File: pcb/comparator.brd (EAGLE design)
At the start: 15.9 x 15.6 mm, 13 parts, among them U1 MAX9032

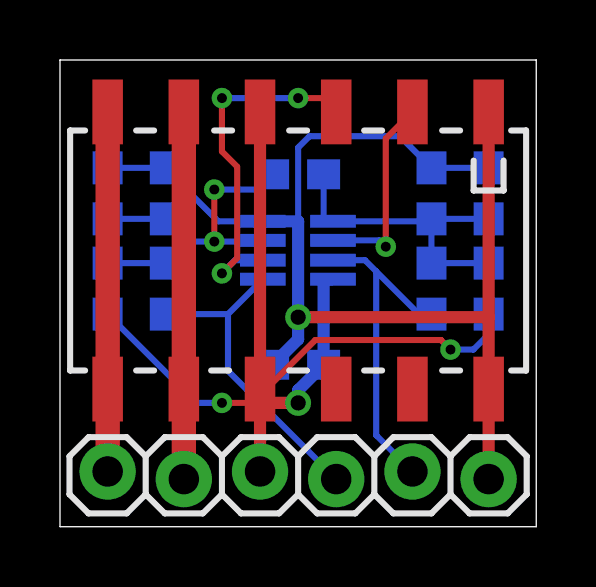
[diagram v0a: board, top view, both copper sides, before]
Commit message: Tweaked encoder conditiner board
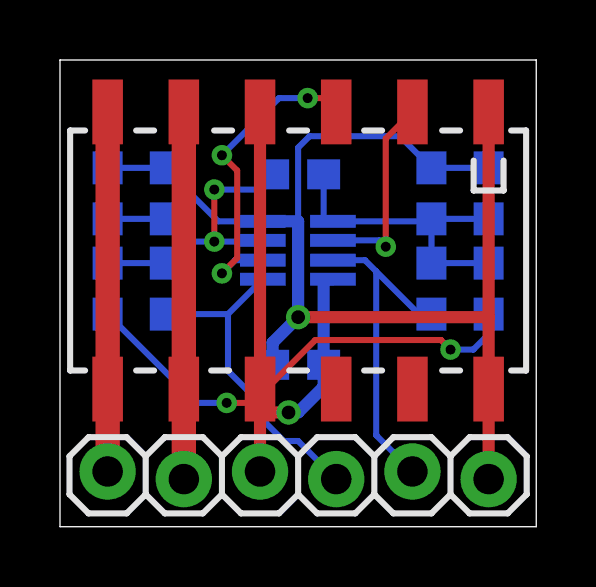
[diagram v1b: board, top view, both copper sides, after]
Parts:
- turned R4 to 90 degrees
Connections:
- net 3.3V: now also R4.1; no longer R4.2
- net N$6: now also R4.2; no longer R4.1
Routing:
- net EN2I: track 12.1 -> 11.0 mm
- net 3.3V: track 34.0 -> 34.8 mm
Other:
- board text added: "Encoder Conditioner"
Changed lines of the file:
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@@
 <setting verticaltext="up"/>
 </settings>
-<grid distance="0.05" unitdist="inch" unit="inch" style="lines" multiple="1" display="no" altdistance="0.0125" altunitdist="inch" altunit="inch"/>
+<grid distance="0.05" unitdist="inch" unit="inch" style="lines" multiple="1" display="no" altdistance="0.00625" altunitdist="inch" altunit="inch"/>
 <layers>
 <layer number="1" name="Top" color="4" fill="1" visible="yes" active="yes"/>
@@
 <wire x1="15.875" y1="15.5575" x2="0" y2="15.5575" width="0" layer="20"/>
 <wire x1="0" y1="15.5575" x2="0" y2="0" width="0" layer="20"/>
-<text x="14.2875" y="4.7625" size="0.8128" layer="22" rot="SMR270" align="center">GND</text>
-<text x="12.7" y="14.2875" size="0.8128" layer="22" rot="MR0" align="center">MAX9032</text>
+<text x="14.2875" y="4.445" size="0.8128" layer="22" rot="SMR270" align="center">GND</text>
+<text x="10.4775" y="6.6675" size="0.6096" layer="22" rot="MR270" align="center">MAX9032</text>
+<text x="11.7475" y="13.97" size="0.8128" layer="22" rot="MR0" align="center">Encoder
+Conditioner</text>
 </plain>
 <attributes>
@@
 </element>
 <element name="U1" library="Custom" package="SOT23-8" value="MAX9032" x="7.9375" y="9.2075" smashed="yes" rot="MR180">
-<attribute name="NAME" x="6.96514375" y="7.309653125" size="0.8128" layer="26" ratio="10" rot="SMR180"/>
+<attribute name="NAME" x="8.55264375" y="7.627153125" size="0.6096" layer="26" ratio="10" rot="SMR180"/>
 </element>
 <element name="R1" library="SparkFun-Resistors" package="0603-RES" value="10K" x="1.5875" y="7.9375" rot="MR270"/>
 <element name="R2" library="SparkFun-Resistors" package="0603-RES" value="3.3K" x="3.4925" y="11.1125" rot="MR90"/>
 <element name="R3" library="SparkFun-Resistors" package="0603-RES" value="100K" x="3.4925" y="7.9375" rot="MR90"/>
-<element name="R4" library="SparkFun-Resistors" package="0603-RES" value="10K" x="14.2875" y="7.9375" rot="MR270"/>
+<element name="R4" library="SparkFun-Resistors" package="0603-RES" value="10K" x="14.2875" y="7.9375" rot="MR90"/>
 <element name="R5" library="SparkFun-Resistors" package="0603-RES" value="3.3K" x="12.3825" y="11.1125" rot="MR270"/>
 <element name="R6" library="SparkFun-Resistors" package="0603-RES" value="100K" x="12.3825" y="7.9375" rot="MR270"/>
@@
 <element name="C2" library="SparkFun-Capacitors" package="0603-CAP" value="" x="14.2875" y="11.1125" rot="MR90"/>
 <element name="C3" library="SparkFun-Capacitors" package="0603-CAP" value="0.1uF" x="7.9375" y="5.3975" rot="MR0"/>
-<element name="R7" library="SparkFun-Resistors" package="0603-RES" value="0" x="7.9375" y="11.7475" rot="MR0"/>
+<element name="R7" library="SparkFun-Resistors" package="0603-RES" value="0" x="7.9375" y="11.7475" smashed="yes" rot="MR0">
+<attribute name="NAME" x="7.5565" y="12.5095" size="0.4064" layer="26" font="vector" rot="MR0"/>
+<attribute name="VALUE" x="8.9535" y="10.6045" size="0.4064" layer="28" font="vector" rot="MR0"/>
+</element>
 </elements>
 <signals>
@@
 <via x="5.3975" y="8.4455" extent="1-16" drill="0.3302"/>
 <wire x1="5.3975" y1="8.4455" x2="5.9055" y2="8.9535" width="0.2032" layer="1"/>
-<wire x1="5.9055" y1="8.9535" x2="5.9055" y2="12.0015" width="0.2032" layer="1"/>
-<wire x1="5.9055" y1="12.0015" x2="5.3975" y2="12.5095" width="0.2032" layer="1"/>
-<wire x1="5.3975" y1="12.5095" x2="5.3975" y2="14.2875" width="0.2032" layer="1"/>
-<via x="5.3975" y="14.2875" extent="1-16" drill="0.3302"/>
-<wire x1="5.3975" y1="14.2875" x2="7.9375" y2="14.2875" width="0.2032" layer="16"/>
-<via x="7.9375" y="14.2875" extent="1-16" drill="0.3302"/>
-<wire x1="7.9375" y1="14.2875" x2="9.2075" y2="14.2875" width="0.2032" layer="1"/>
+<via x="8.255" y="14.2875" extent="1-16" drill="0.3302"/>
+<wire x1="8.255" y1="14.2875" x2="9.2075" y2="14.2875" width="0.2032" layer="1"/>
 <wire x1="9.2075" y1="14.2875" x2="9.2075" y2="13.8275" width="0.2032" layer="1"/>
+<wire x1="5.9055" y1="8.9535" x2="5.9055" y2="11.8745" width="0.2032" layer="1"/>
+<wire x1="5.9055" y1="11.8745" x2="5.3975" y2="12.3825" width="0.2032" layer="1"/>
+<via x="5.3975" y="12.3825" extent="1-16" drill="0.3302"/>
+<wire x1="5.3975" y1="12.3825" x2="7.3025" y2="14.2875" width="0.2032" layer="16"/>
+<wire x1="7.3025" y1="14.2875" x2="8.255" y2="14.2875" width="0.2032" layer="16"/>
 </signal>
 <signal name="EN1I">
@@
 <wire x1="3.4925" y1="7.0875" x2="5.599990625" y2="7.0875" width="0.2032" layer="16"/>
 <wire x1="5.599990625" y1="7.0875" x2="6.76194375" y2="8.249453125" width="0.2032" layer="16"/>
-<wire x1="9.2075" y1="1.5875" x2="5.599990625" y2="5.195009375" width="0.2032" layer="16"/>
 <wire x1="5.599990625" y1="5.195009375" x2="5.599990625" y2="7.0875" width="0.2032" layer="16"/>
+<wire x1="5.599990625" y1="5.195009375" x2="6.6675" y2="4.1275" width="0.2032" layer="16"/>
+<wire x1="6.6675" y1="4.1275" x2="6.6675" y2="3.65125" width="0.2032" layer="16"/>
+<wire x1="6.6675" y1="3.65125" x2="7.46125" y2="2.8575" width="0.2032" layer="16"/>
+<wire x1="7.46125" y1="2.8575" x2="7.9375" y2="2.8575" width="0.2032" layer="16"/>
+<wire x1="7.9375" y1="2.8575" x2="9.2075" y2="1.5875" width="0.2032" layer="16"/>
 </signal>
 <signal name="EN1O">
@@
 <contactref element="U1" pad="8"/>
 <contactref element="R1" pad="2"/>
-<contactref element="R4" pad="2"/>
+<contactref element="R4" pad="1"/>
 <contactref element="C3" pad="1"/>
 <wire x1="6.6675" y1="13.8275" x2="6.6675" y2="4.1275" width="0.4064" layer="1"/>
 <wire x1="6.6675" y1="4.1275" x2="6.6675" y2="1.8415" width="0.4064" layer="1"/>
-<wire x1="8.7875" y1="5.3975" x2="7.9375" y2="4.5475" width="0.4064" layer="16"/>
-<wire x1="7.9375" y1="4.5475" x2="7.9375" y2="4.1275" width="0.4064" layer="16"/>
-<via x="7.9375" y="4.1275" extent="1-16" drill="0.508"/>
-<wire x1="7.9375" y1="4.1275" x2="6.731" y2="4.1275" width="0.4064" layer="1"/>
 <wire x1="6.731" y1="4.1275" x2="6.6675" y2="4.1275" width="0.4064" layer="1"/>
 <wire x1="8.7875" y1="5.3975" x2="8.7875" y2="8.249453125" width="0.4064" layer="16"/>
 <wire x1="8.7875" y1="8.249453125" x2="9.09874375" y2="8.249453125" width="0.4064" layer="16"/>
 <wire x1="1.5875" y1="7.0875" x2="4.5475" y2="4.1275" width="0.2032" layer="16"/>
-<wire x1="4.5475" y1="4.1275" x2="5.3975" y2="4.1275" width="0.2032" layer="16"/>
-<via x="5.3975" y="4.1275" extent="1-16" drill="0.3302"/>
-<wire x1="5.3975" y1="4.1275" x2="6.6675" y2="4.1275" width="0.2032" layer="1"/>
+<wire x1="4.5475" y1="4.1275" x2="5.55625" y2="4.1275" width="0.2032" layer="16"/>
+<via x="5.55625" y="4.1275" extent="1-16" drill="0.3302"/>
+<wire x1="5.55625" y1="4.1275" x2="6.6675" y2="4.1275" width="0.2032" layer="1"/>
 <via x="13.0175" y="5.9055" extent="1-16" drill="0.3302"/>
 <wire x1="13.0175" y1="5.9055" x2="12.7" y2="6.223" width="0.2032" layer="1"/>
@@
 <wire x1="14.2875" y1="6.4135" x2="13.7795" y2="5.9055" width="0.2032" layer="16"/>
 <wire x1="13.7795" y1="5.9055" x2="13.0175" y2="5.9055" width="0.2032" layer="16"/>
+<wire x1="8.89" y1="5.08" x2="8.89" y2="5.295" width="0.4064" layer="16"/>
+<wire x1="8.89" y1="5.295" x2="8.7875" y2="5.3975" width="0.4064" layer="16"/>
+<via x="7.62" y="3.81" extent="1-16" drill="0.4572"/>
+<wire x1="7.62" y1="3.81" x2="7.0485" y2="3.81" width="0.4064" layer="1"/>
+<wire x1="7.0485" y1="3.81" x2="6.731" y2="4.1275" width="0.4064" layer="1"/>
+<wire x1="7.62" y1="3.81" x2="7.9375" y2="3.81" width="0.4064" layer="16"/>
+<wire x1="7.9375" y1="3.81" x2="8.7875" y2="4.66" width="0.4064" layer="16"/>
+<wire x1="8.7875" y1="4.66" x2="8.7875" y2="5.3975" width="0.4064" layer="16"/>
 </signal>
 <signal name="GND">
@@
 <wire x1="14.2875" y1="13.8275" x2="14.2875" y2="6.985" width="0.4064" layer="1"/>
 <wire x1="14.2875" y1="6.985" x2="14.2875" y2="1.5875" width="0.4064" layer="1"/>
-<wire x1="7.0875" y1="5.3975" x2="7.9375" y2="6.2475" width="0.4064" layer="16"/>
-<wire x1="7.9375" y1="6.2475" x2="7.9375" y2="6.985" width="0.4064" layer="16"/>
-<via x="7.9375" y="6.985" extent="1-16" drill="0.508"/>
+<via x="7.9375" y="6.985" extent="1-16" drill="0.4572"/>
 <wire x1="7.9375" y1="6.985" x2="14.2875" y2="6.985" width="0.4064" layer="1"/>
 <wire x1="7.9375" y1="6.985" x2="7.9375" y2="10.179853125" width="0.4064" layer="16"/>
@@
 <wire x1="7.9375" y1="12.6365" x2="7.9375" y2="10.179853125" width="0.2032" layer="16"/>
 <wire x1="14.2875" y1="11.9625" x2="12.3825" y2="11.9625" width="0.2032" layer="16"/>
+<wire x1="7.0875" y1="5.3975" x2="7.0875" y2="6.135" width="0.4064" layer="16"/>
+<wire x1="7.0875" y1="6.135" x2="7.9375" y2="6.985" width="0.4064" layer="16"/>
 </signal>
 <signal name="N$3">
@@
 <contactref element="U1" pad="5"/>
 <contactref element="R5" pad="2"/>
-<contactref element="R4" pad="1"/>
+<contactref element="R4" pad="2"/>
 <contactref element="C2" pad="1"/>
 <contactref element="R7" pad="1"/>
@@
 </board>
 </drawing>
+<compatibility>
+<note version="6.3" minversion="6.2.2" severity="warning">
+Since Version 6.2.2 text objects can contain more than one line,
+which will not be processed correctly with this version.
+</note>
+</compatibility>
 </eagle>

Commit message: Specified capacitor value on comparator boards
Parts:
- C1, C2: value (none) -> 1nF
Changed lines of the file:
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@@
 <element name="R5" library="SparkFun-Resistors" package="0603-RES" value="3.3K" x="12.3825" y="11.1125" rot="MR270"/>
 <element name="R6" library="SparkFun-Resistors" package="0603-RES" value="100K" x="12.3825" y="7.9375" rot="MR270"/>
-<element name="C1" library="SparkFun-Capacitors" package="0603-CAP" value="" x="1.5875" y="11.1125" rot="MR270"/>
-<element name="C2" library="SparkFun-Capacitors" package="0603-CAP" value="" x="14.2875" y="11.1125" rot="MR90"/>
+<element name="C1" library="SparkFun-Capacitors" package="0603-CAP" value="1nF" x="1.5875" y="11.1125" rot="MR270"/>
+<element name="C2" library="SparkFun-Capacitors" package="0603-CAP" value="1nF" x="14.2875" y="11.1125" rot="MR90"/>
 <element name="C3" library="SparkFun-Capacitors" package="0603-CAP" value="0.1uF" x="7.9375" y="5.3975" rot="MR0"/>
 <element name="R7" library="SparkFun-Resistors" package="0603-RES" value="0" x="7.9375" y="11.7475" smashed="yes" rot="MR0">
